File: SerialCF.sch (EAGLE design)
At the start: 7 parts, among them IC4 XR-16C550P

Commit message: Finish Modularization
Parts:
- removed V3: 74HC00N, 74ttl-din:74HC00N
- added JP1: (no value), jean:JEANNECTOR/90
- added LED1: AC, led:LED5MM
- added R2: 560, resistor:R-EU_0204/7
- SV2: value IDE PATA -> IDE PATA CF Card
- V2: MF TEXAS INSTRUMENTS -> (none); MPN SN74HC00N -> (none); OC_FARNELL 9590889 -> (none)
- renumbered IC4 to IC1
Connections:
- removed net CLOCK: IC1G$1.XTAL1
- new net A10: JP1.A10
- new net A11: JP1.A11
- new net A12: JP1.A12
- new net A13: JP1.A13
- new net A14: JP1.A14
- new net A15: JP1.A15
- new net A3: JP1.A3
- new net A4: JP1.A4
- new net A5: JP1.A5
- new net A6: JP1.A6, V2/2.A, V2/2.B, V2/3.A, V2/3.B
- new net A8: JP1.A8
- new net A9: JP1.A9
- new net N$1: IC1G$1.XTAL1, JP1.CLK
- new net N$2: LED1.C, SV2.39
- new net N$3: LED1.A, R2.1
- new net N$4: V1/1.Y, V2/1.B
- new net N$5: V2/1.A, V2/2.Y
- new net N$6: V2/3.Y, V2/4.B
- new net N$7: V1/4.Y, V2/4.A
- net !RESET: now also JP1.!RESET, V1/2.A, V1/2.B
- net A0: now also JP1.A0
- net A1: now also JP1.A1
- net A2: now also JP1.A2
- net A7: now also JP1.A7, V1/1.A, V1/3.A, V1/3.B; no longer V3/1.A, V3/1.B
- net D0: now also JP1.D0
- net D1: now also JP1.D1
- net D2: now also JP1.D2
- net D3: now also JP1.D3
- net D4: now also JP1.D4
- net D5: now also JP1.D5
- net D6: now also JP1.D6
- net D7: now also JP1.D7
- net GND: now also JP1.GND@1, JP1.GND@2, V1/-UB.-UB
- net N$17: now also V1/3.Y, V1/4.B; no longer V2/4.B, V3/1.Y
- net N$18: now also V2/1.Y; no longer V2/3.Y
- net N$19: now also JP1.!IOREQ, V1/1.B, V1/4.A; no longer V2/4.A
- net RESET: now also V1/2.Y
- net VCC: now also JP1.VCC, R2.2, V1/+UB.+UB
- net WAIT: now also JP1.!WAIT
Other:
- note added: "A7 = 0 A6 = 0"
- note added: "A7 = 0 A6 = 1"
- note removed: "A7 = 0"
- note removed: "A7 = 1"
- moved on the sheet: V1/2, V2/3, V2/4

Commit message: Add Interrupt connection for 16550
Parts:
- added R3: 100k, resistor:R-EU_0207/2V
- added R4: 3.3k, resistor:R-EU_0207/2V
- added T1: BC547, transistor:BC547
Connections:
- new net N$10: IC1G$1.INT, R3.1
- new net N$8: R3.2, T1.B
- new net N$9: JP1.!INT, R4.1, T1.C
- net GND: now also T1.E
- net VCC: now also R4.2
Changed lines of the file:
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@@
 <part name="P+3" library="supply1" deviceset="VCC" device=""/>
 <part name="V2" library="74ttl-din" deviceset="74*00" device="N" technology="HC"/>
+<part name="T1" library="transistor" deviceset="BC547" device=""/>
+<part name="R3" library="resistor" deviceset="R-EU_" device="0207/2V" value="100k"/>
+<part name="R4" library="resistor" deviceset="R-EU_" device="0207/2V" value="3.3k"/>
+<part name="P+4" library="supply1" deviceset="VCC" device=""/>
+<part name="GND4" library="supply1" deviceset="GND" device=""/>
 </parts>
 <sheets>
@@
 <instance part="V2" gate="/3" x="276.86" y="71.12"/>
 <instance part="V2" gate="/4" x="297.18" y="73.66"/>
+<instance part="T1" gate="G$1" x="200.66" y="-66.04"/>
+<instance part="R3" gate="G$1" x="190.5" y="-66.04"/>
+<instance part="R4" gate="G$1" x="203.2" y="-55.88" rot="R90"/>
+<instance part="P+4" gate="VCC" x="203.2" y="-48.26"/>
+<instance part="GND4" gate="1" x="203.2" y="-73.66"/>
 </instances>
 <busses>
@@
 <pinref part="P+3" gate="VCC" pin="VCC"/>
 <wire x1="307.34" y1="-17.78" x2="307.34" y2="-20.32" width="0.1524" layer="91"/>
+</segment>
+<segment>
+<pinref part="R4" gate="G$1" pin="2"/>
+<pinref part="P+4" gate="VCC" pin="VCC"/>
 </segment>
 </net>
@@
 <wire x1="58.42" y1="-12.7" x2="58.42" y2="-15.24" width="0.1524" layer="91"/>
 </segment>
+<segment>
+<pinref part="T1" gate="G$1" pin="E"/>
+<pinref part="GND4" gate="1" pin="GND"/>
+</segment>
 </net>
 <net name="!WR" class="0">
@@
 </segment>
 </net>
+<net name="N$8" class="0">
+<segment>
+<pinref part="T1" gate="G$1" pin="B"/>
+<pinref part="R3" gate="G$1" pin="2"/>
+<wire x1="198.12" y1="-66.04" x2="195.58" y2="-66.04" width="0.1524" layer="91"/>
+</segment>
+</net>
+<net name="N$9" class="0">
+<segment>
+<pinref part="T1" gate="G$1" pin="C"/>
+<pinref part="R4" gate="G$1" pin="1"/>
+<wire x1="203.2" y1="-60.96" x2="218.44" y2="-60.96" width="0.1524" layer="91"/>
+<wire x1="218.44" y1="-60.96" x2="218.44" y2="-83.82" width="0.1524" layer="91"/>
+<junction x="203.2" y="-60.96"/>
+<wire x1="218.44" y1="-83.82" x2="43.18" y2="-83.82" width="0.1524" layer="91"/>
+<wire x1="43.18" y1="-83.82" x2="43.18" y2="5.08" width="0.1524" layer="91"/>
+<pinref part="JP1" gate="A" pin="!INT"/>
+<wire x1="43.18" y1="5.08" x2="66.04" y2="5.08" width="0.1524" layer="91"/>
+</segment>
+</net>
+<net name="N$10" class="0">
+<segment>
+<pinref part="R3" gate="G$1" pin="1"/>
+<wire x1="185.42" y1="-66.04" x2="180.34" y2="-66.04" width="0.1524" layer="91"/>
+<wire x1="180.34" y1="-66.04" x2="180.34" y2="-12.7" width="0.1524" layer="91"/>
+<wire x1="180.34" y1="-12.7" x2="190.5" y2="-12.7" width="0.1524" layer="91"/>
+<wire x1="190.5" y1="-12.7" x2="190.5" y2="7.62" width="0.1524" layer="91"/>
+<pinref part="IC1" gate="G$1" pin="INT"/>
+<wire x1="190.5" y1="7.62" x2="182.88" y2="7.62" width="0.1524" layer="91"/>
+</segment>
+</net>

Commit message: Add Decoupling Capacitors.
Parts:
- added C1, C2, C3, C4: 0.1µF, capacitor-wima:C5/2.5
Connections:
- net GND: now also C1.2, C2.2, C3.2, C4.2
- net VCC: now also C1.1, C2.1, C3.1, C4.1
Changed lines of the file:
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@@
 <part name="P+4" library="supply1" deviceset="VCC" device=""/>
 <part name="GND4" library="supply1" deviceset="GND" device=""/>
+<part name="C1" library="capacitor-wima" deviceset="C" device="5/2.5" value="0.1µF"/>
+<part name="P+5" library="supply1" deviceset="VCC" device=""/>
+<part name="GND5" library="supply1" deviceset="GND" device=""/>
+<part name="C2" library="capacitor-wima" deviceset="C" device="5/2.5" value="0.1µF"/>
+<part name="P+7" library="supply1" deviceset="VCC" device=""/>
+<part name="GND6" library="supply1" deviceset="GND" device=""/>
+<part name="C3" library="capacitor-wima" deviceset="C" device="5/2.5" value="0.1µF"/>
+<part name="P+10" library="supply1" deviceset="VCC" device=""/>
+<part name="GND8" library="supply1" deviceset="GND" device=""/>
+<part name="C4" library="capacitor-wima" deviceset="C" device="5/2.5" value="0.1µF"/>
+<part name="P+11" library="supply1" deviceset="VCC" device=""/>
+<part name="GND9" library="supply1" deviceset="GND" device=""/>
 </parts>
 <sheets>
@@
 <instance part="P+4" gate="VCC" x="203.2" y="-48.26"/>
 <instance part="GND4" gate="1" x="203.2" y="-73.66"/>
+<instance part="C1" gate="G$1" x="215.9" y="40.64"/>
+<instance part="P+5" gate="VCC" x="215.9" y="45.72"/>
+<instance part="GND5" gate="1" x="215.9" y="33.02"/>
+<instance part="C2" gate="G$1" x="314.96" y="38.1"/>
+<instance part="P+7" gate="VCC" x="314.96" y="43.18"/>
+<instance part="GND6" gate="1" x="314.96" y="30.48"/>
+<instance part="C3" gate="G$1" x="307.34" y="91.44"/>
+<instance part="P+10" gate="VCC" x="307.34" y="96.52"/>
+<instance part="GND8" gate="1" x="307.34" y="83.82"/>
+<instance part="C4" gate="G$1" x="223.52" y="111.76"/>
+<instance part="P+11" gate="VCC" x="223.52" y="116.84"/>
+<instance part="GND9" gate="1" x="223.52" y="104.14"/>
 </instances>
 <busses>
@@
 <pinref part="R4" gate="G$1" pin="2"/>
 <pinref part="P+4" gate="VCC" pin="VCC"/>
+</segment>
+<segment>
+<pinref part="C1" gate="G$1" pin="1"/>
+<pinref part="P+5" gate="VCC" pin="VCC"/>
+</segment>
+<segment>
+<pinref part="C2" gate="G$1" pin="1"/>
+<pinref part="P+7" gate="VCC" pin="VCC"/>
+</segment>
+<segment>
+<pinref part="C3" gate="G$1" pin="1"/>
+<pinref part="P+10" gate="VCC" pin="VCC"/>
+</segment>
+<segment>
+<pinref part="C4" gate="G$1" pin="1"/>
+<pinref part="P+11" gate="VCC" pin="VCC"/>
 </segment>
 </net>
@@
 <pinref part="GND4" gate="1" pin="GND"/>
 </segment>
-</net>
+<segment>
+<pinref part="C1" gate="G$1" pin="2"/>
+<pinref part="GND5" gate="1" pin="GND"/>
+</segment>
+<segment>
+<pinref part="C2" gate="G$1" pin="2"/>
+<pinref part="GND6" gate="1" pin="GND"/>
+</segment>
+<segment>
+<pinref part="C3" gate="G$1" pin="2"/>
+<pinref part="GND8" gate="1" pin="GND"/>
+</segment>
+<segment>
+<pinref part="C4" gate="G$1" pin="2"/>
+<pinref part="GND9" gate="1" pin="GND"/>
+</segment>
+</net>

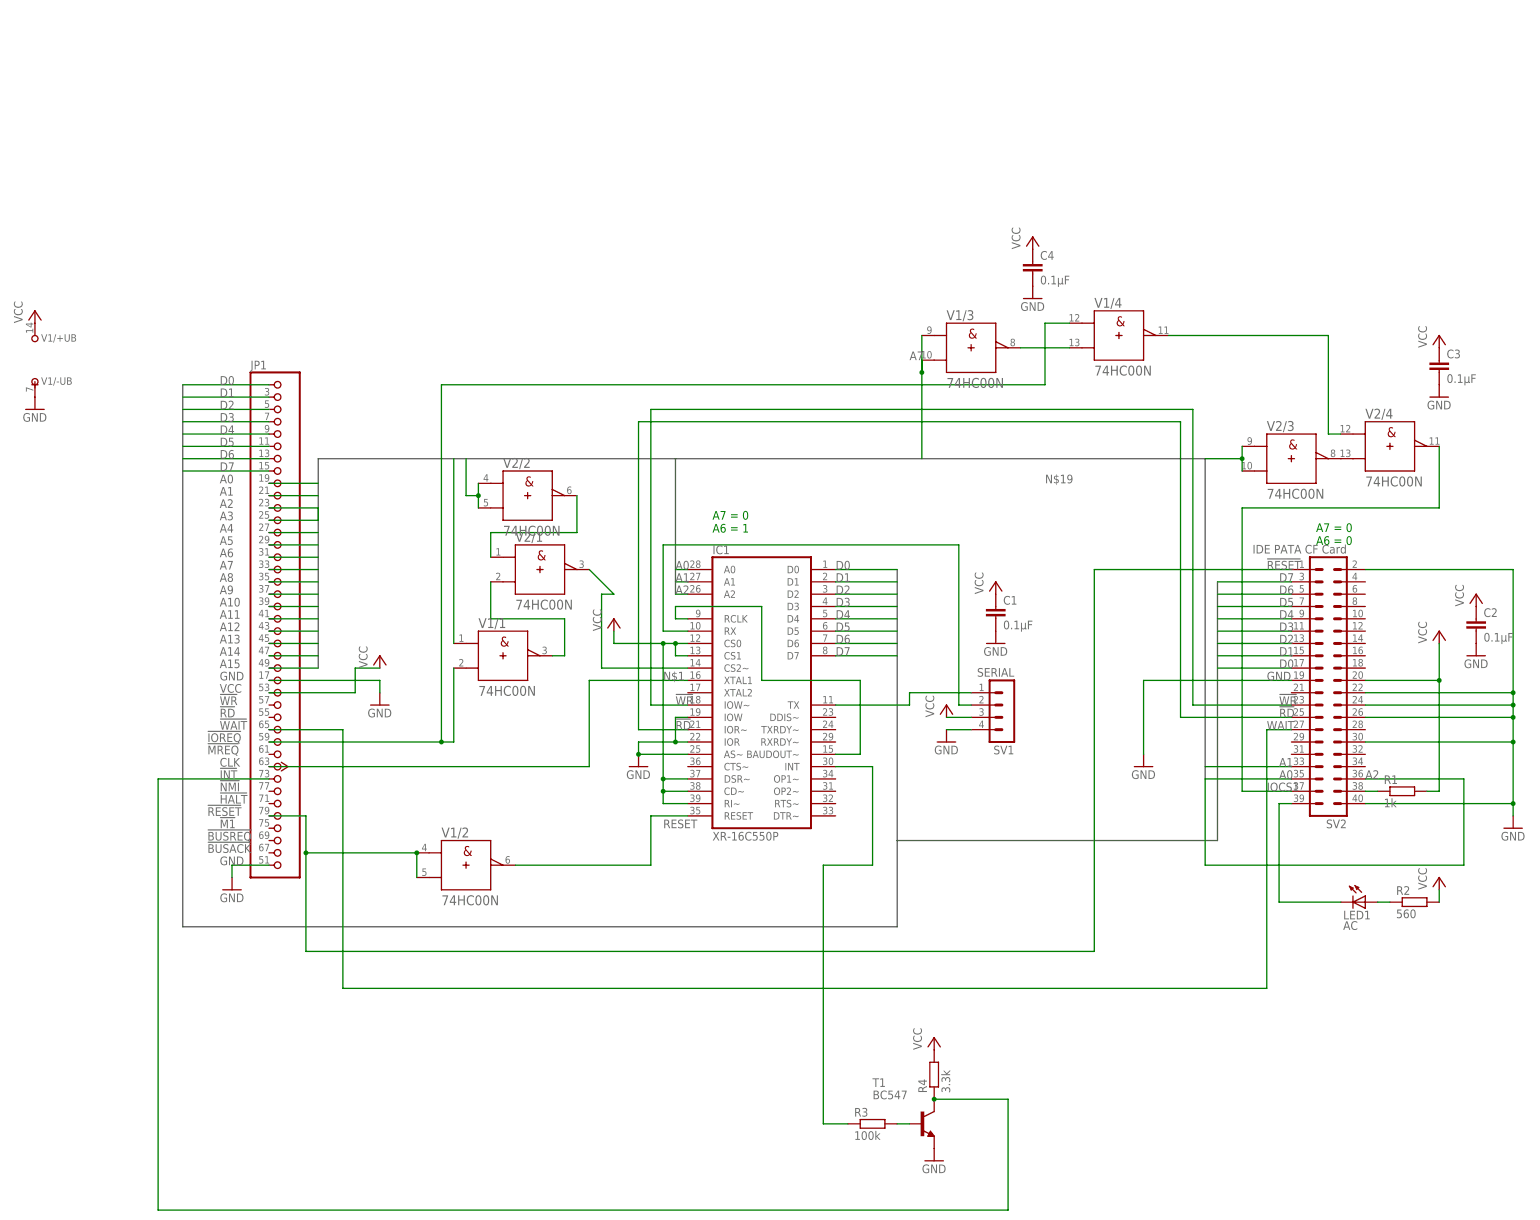
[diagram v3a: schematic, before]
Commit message: Change addressbus to allow more devices on it.
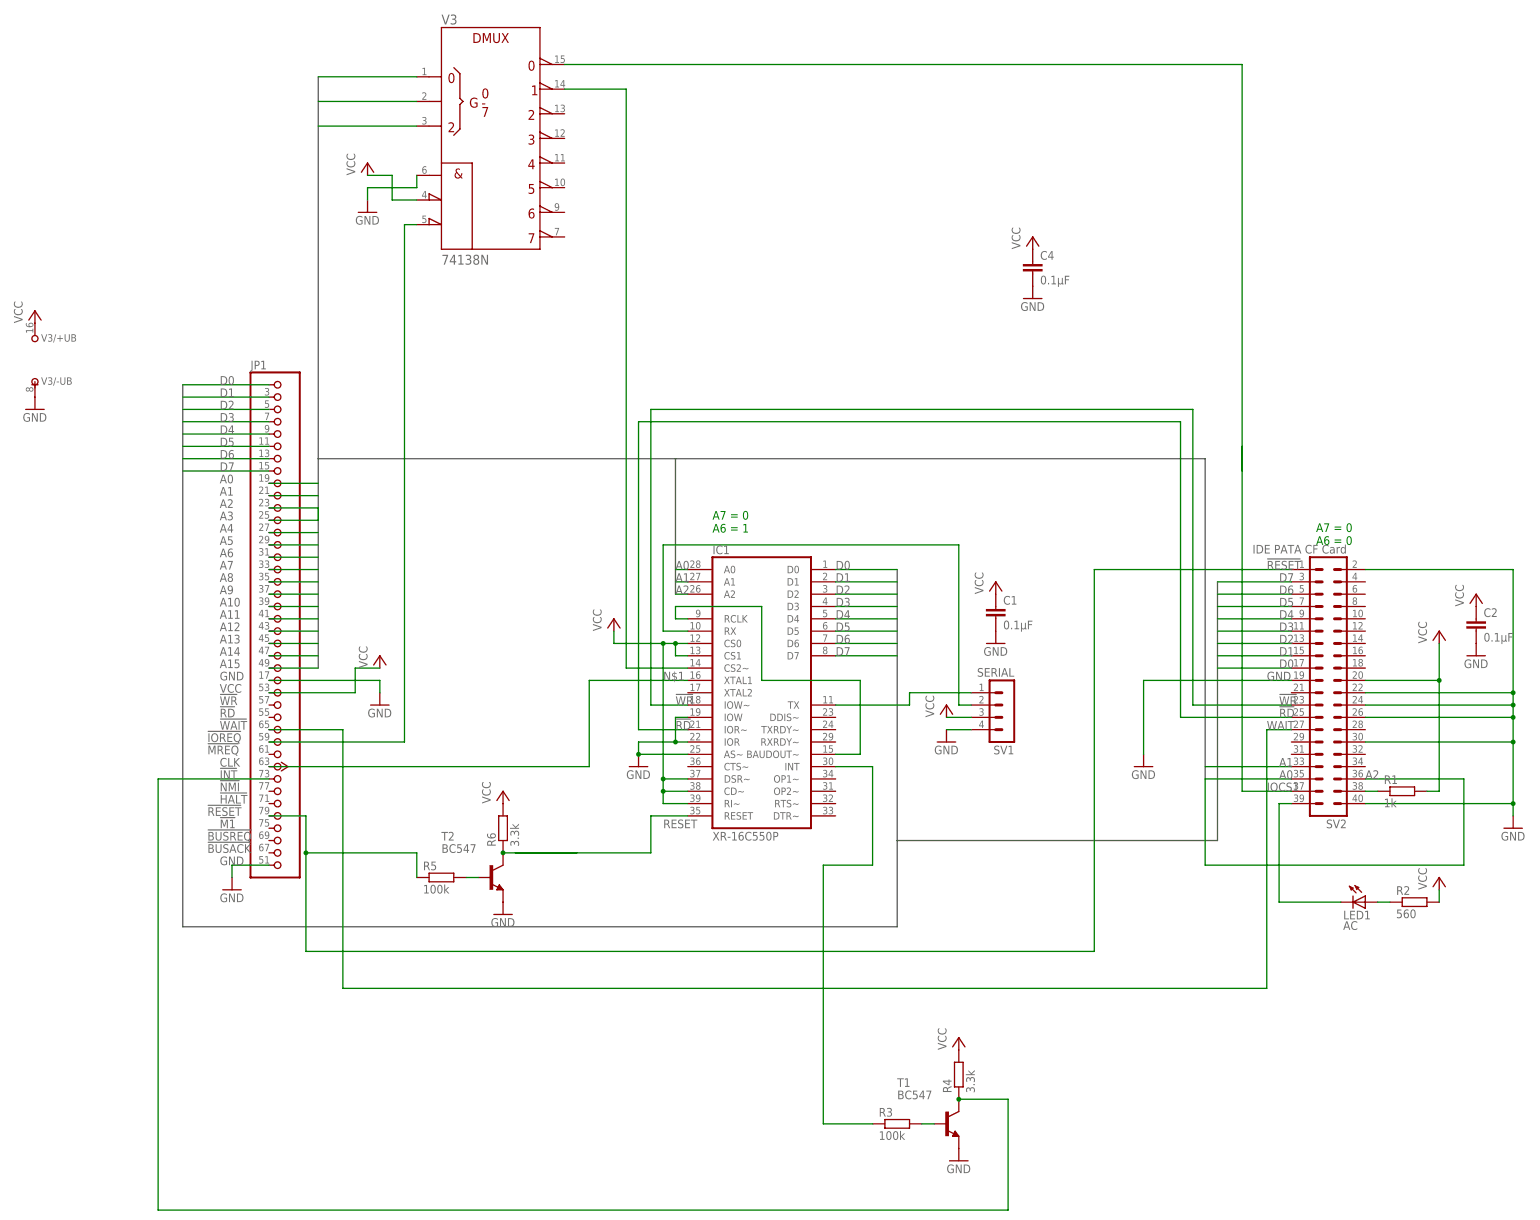
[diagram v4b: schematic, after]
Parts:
- removed C3: 0.1µF, capacitor-wima:C5/2.5
- removed V1, V2: 74HC00N, 74ttl-din:74HC00N
- added R5: 100k, resistor:R-EU_0207/2V
- added R6: 3.3k, resistor:R-EU_0207/2V
- added T2: BC547, transistor:BC547
- added V3: 74138N, 74ttl-din:74138N
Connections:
- removed net N$17: V1/3.Y, V1/4.B
- removed net N$18: IC1G$1.CS2~, V2/1.Y
- removed net N$19: JP1.!IOREQ, V1/1.B, V1/4.A
- net !RESET: no longer V1/2.A, V1/2.B
- net A5: now also V31.A
- net A6: now also V31.B; no longer V2/2.A, V2/2.B, V2/3.A, V2/3.B
- net A7: now also V31.C; no longer V1/1.A, V1/3.A, V1/3.B
- net GND: now also T2.E, V3/-UB.-UB, V31.G1; no longer C3.2, V1/-UB.-UB
- net IOCS1: now also V31.Y0; no longer V2/4.Y
- net N$4: now also IC1G$1.CS2~, V31.Y1; no longer V1/1.Y, V2/1.B
- net N$5: now also JP1.!IOREQ, V31.!G2B; no longer V2/1.A, V2/2.Y
- net N$6: now also R5.2, T2.B; no longer V2/3.Y, V2/4.B
- net N$7: now also R6.1, T2.C; no longer V1/4.Y, V2/4.A
- net RESET: no longer V1/2.Y
- net VCC: now also R6.2, V3/+UB.+UB, V31.!G2A; no longer C3.1, V1/+UB.+UB
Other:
- moved on the sheet: R3, R4, T1

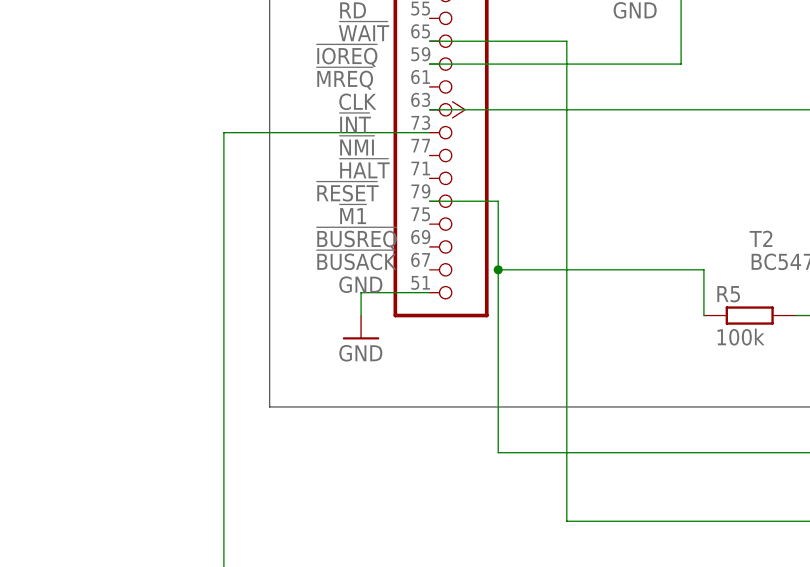
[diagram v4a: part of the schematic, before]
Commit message: Add Ground Rail to JEANNECTOR
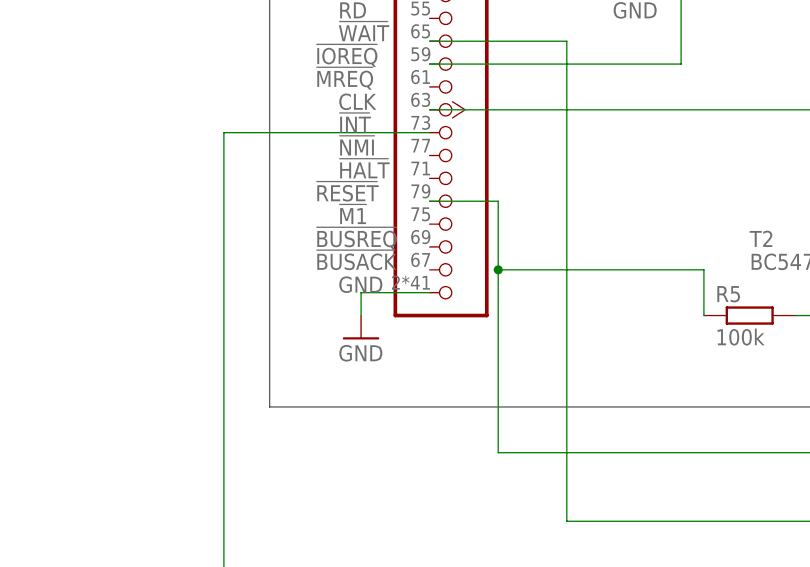
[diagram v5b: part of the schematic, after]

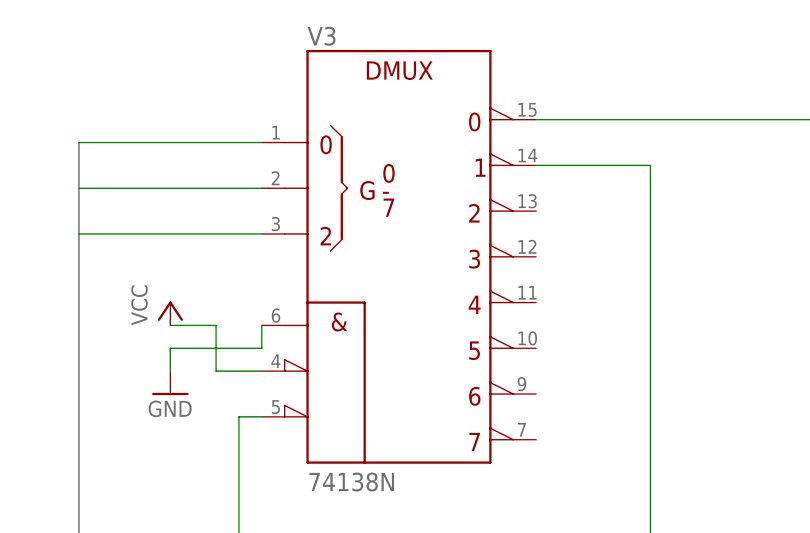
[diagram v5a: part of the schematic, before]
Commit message: Update SerialCF Picture
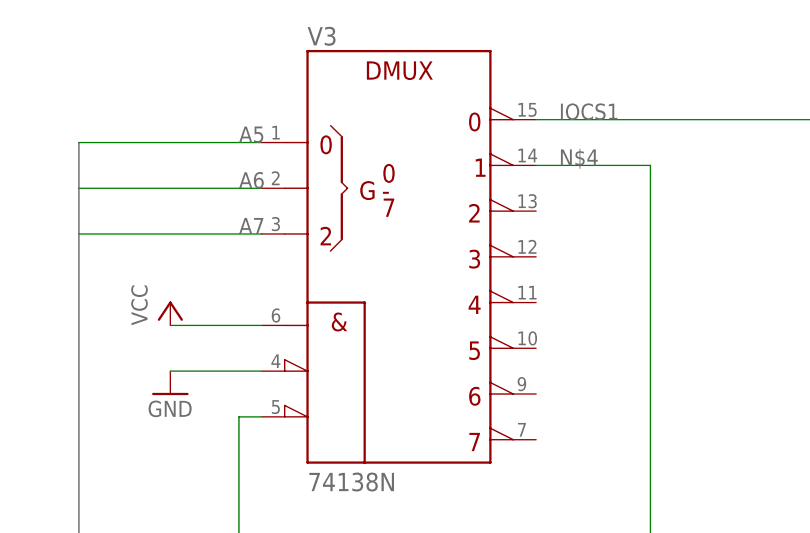
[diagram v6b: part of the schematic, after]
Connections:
- net GND: now also V31.!G2A; no longer V31.G1
- net VCC: now also V31.G1; no longer V31.!G2A
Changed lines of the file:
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@@
 <pinref part="V3" gate="1" pin="C"/>
 <wire x1="96.52" y1="139.7" x2="76.2" y2="139.7" width="0.1524" layer="91"/>
+<label x="93.98" y="139.7" size="1.778" layer="95"/>
 </segment>
 </net>
@@
 <segment>
 <pinref part="P+12" gate="VCC" pin="VCC"/>
-<wire x1="86.36" y1="129.54" x2="91.44" y2="129.54" width="0.1524" layer="91"/>
-<wire x1="91.44" y1="129.54" x2="91.44" y2="124.46" width="0.1524" layer="91"/>
-<pinref part="V3" gate="1" pin="!G2A"/>
-<wire x1="91.44" y1="124.46" x2="96.52" y2="124.46" width="0.1524" layer="91"/>
+<pinref part="V3" gate="1" pin="G1"/>
+<wire x1="86.36" y1="129.54" x2="96.52" y2="129.54" width="0.1524" layer="91"/>
 </segment>
 <segment>
@@
 </segment>
 <segment>
-<pinref part="GND13" gate="1" pin="GND"/>
-<wire x1="86.36" y1="124.46" x2="86.36" y2="127" width="0.1524" layer="91"/>
-<wire x1="86.36" y1="127" x2="96.52" y2="127" width="0.1524" layer="91"/>
-<pinref part="V3" gate="1" pin="G1"/>
-<wire x1="96.52" y1="127" x2="96.52" y2="129.54" width="0.1524" layer="91"/>
-</segment>
-<segment>
 <pinref part="T2" gate="G$1" pin="E"/>
 <pinref part="GND14" gate="1" pin="GND"/>
+</segment>
+<segment>
+<pinref part="V3" gate="1" pin="!G2A"/>
+<pinref part="GND13" gate="1" pin="GND"/>
+<wire x1="96.52" y1="124.46" x2="86.36" y2="124.46" width="0.1524" layer="91"/>
 </segment>
 </net>
@@
 <wire x1="127" y1="152.4" x2="266.7" y2="152.4" width="0.1524" layer="91"/>
 <wire x1="266.7" y1="2.54" x2="266.7" y2="152.4" width="0.1524" layer="91"/>
+<label x="129.54" y="152.4" size="1.778" layer="95"/>
 </segment>
 </net>
@@
 <pinref part="V3" gate="1" pin="A"/>
 <wire x1="96.52" y1="149.86" x2="76.2" y2="149.86" width="0.1524" layer="91"/>
+<label x="93.98" y="149.86" size="1.778" layer="95"/>
 </segment>
 </net>
@@
 <pinref part="V3" gate="1" pin="B"/>
 <wire x1="96.52" y1="144.78" x2="76.2" y2="144.78" width="0.1524" layer="91"/>
+<label x="93.98" y="144.78" size="1.778" layer="95"/>
 </segment>
 </net>
@@
 <pinref part="V3" gate="1" pin="Y1"/>
 <wire x1="139.7" y1="147.32" x2="127" y2="147.32" width="0.1524" layer="91"/>
-</segment>
-</net>
+<label x="129.54" y="147.32" size="1.778" layer="95"/>
+</segment>
+</net>
